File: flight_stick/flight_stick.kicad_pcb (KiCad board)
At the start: 2 copper layers, 75 x 50 mm, 61 parts, among them J1 Load Cell 1, J10 USB_C_Receptacle_USB2.0, J11 Conn_01x05_Pin, J3 Load Cell 2, J5 Load Cell 3, J7 Conn_01x04_Male, J8 Conn_01x05_Pin, J9 Conn_ST_STDC14, Q4 2N7002, Q5 2N7002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

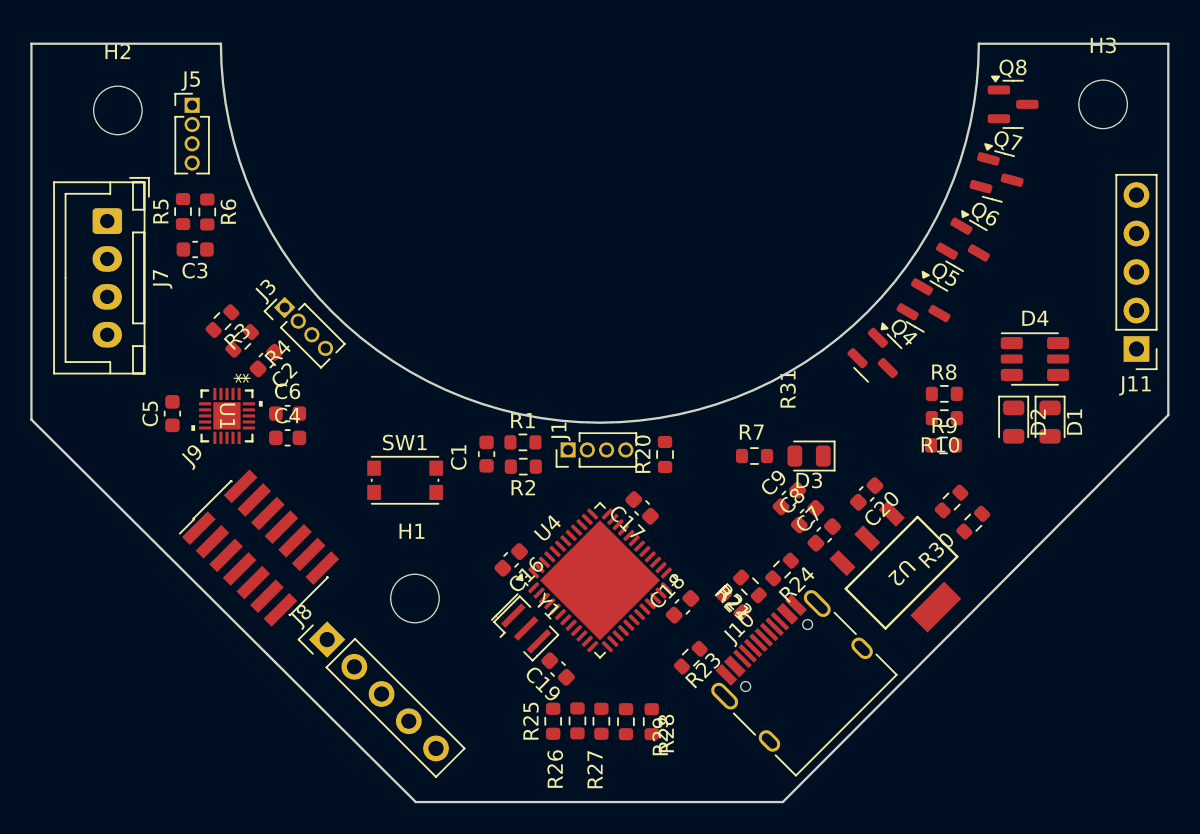
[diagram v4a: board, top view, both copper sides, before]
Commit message: Started on the Routing
layout component placement requires review, traces placed
MCU pins re-assigned
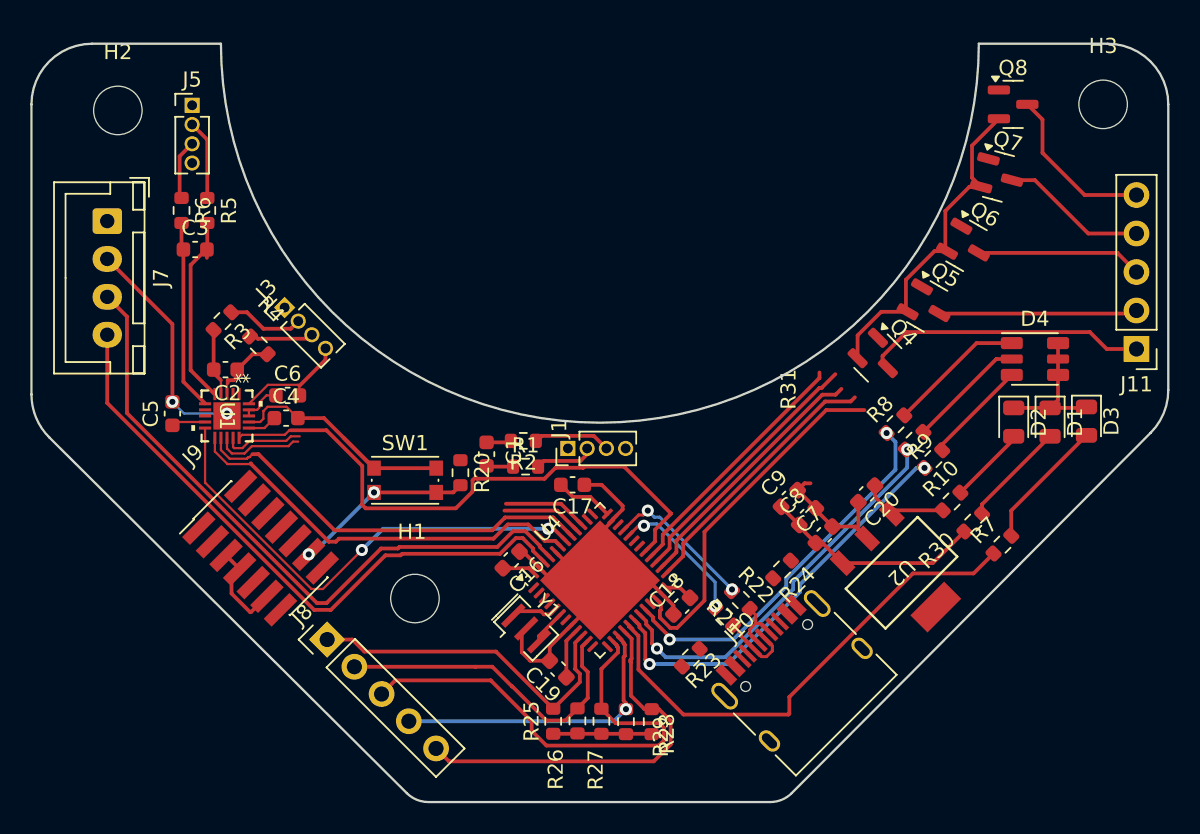
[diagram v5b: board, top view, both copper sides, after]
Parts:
- moved D3 18.4 mm to (179.6, 129.9), turned to -90 degrees
- moved R7 17.4 mm to (174.1, 138.0), turned to 45 degrees
- moved R20 13.6 mm to (138.3, 133.3), turned to -90 degrees
- moved C17 4.83 mm to (145.7, 134.1), turned to 180 degrees
- moved R8 3.79 mm to (167.0, 130.1), turned to 45 degrees
- moved C2 2.77 mm to (122.8, 126.5), turned to 180 degrees
- moved R9 2.47 mm to (168.3, 131.2), turned to 45 degrees
- moved R6 1.70 mm to (119.9, 116.0)
- moved R2 1.70 mm to (142.4, 131.2)
- moved R1 1.61 mm to (142.6, 132.9)
- moved R5 1.60 mm to (121.6, 116.0), turned to -90 degrees
- moved C4 1.30 mm to (126.8, 129.7)
- moved C6 1.20 mm to (126.9, 128.2)
- moved R4 1.14 mm to (125.0, 124.9), turned to -45 degrees
- moved R10 1.13 mm to (169.5, 132.4), turned to 45 degrees
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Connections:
- U4 pad 18: /StatusLED_{B} -> /StatusLED_{G}
- U4 pad 20: /StatusLED_{G} -> /StatusLED_{B}
- U4 pad 22: /Trans1 -> /Trans5
- U4 pad 25: /Trans2 -> /Trans4
- U4 pad 27: /Trans4 -> /Trans2
- U4 pad 28: /Trans5 -> /Trans1
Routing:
- net GND: track 0.00 -> 123.2 mm, vias 0 -> 2
- net /SCL: track 0.00 -> 44.0 mm
- net /SDA: track 0.00 -> 41.7 mm
- net /ADC_MCK: track 0.00 -> 38.5 mm
- net +3.3V: track 0.00 -> 37.3 mm
- net Net-(U4-PA7): track 0.00 -> 32.9 mm
- net /ADC_CS: track 0.00 -> 32.3 mm, vias 0 -> 2
- net /button3: track 0.00 -> 31.8 mm
- net /ADC_DRDY: track 0.00 -> 27.3 mm
- net /ADC_SDI: track 0.00 -> 27.2 mm
- net /StatusLED_{G}: track 0.00 -> 27.1 mm, vias 0 -> 2
- net /StatusLED_{R}: track 0.00 -> 26.1 mm, vias 0 -> 2
- net /button5: track 0.00 -> 25.7 mm
- net /StatusLED_{B}: track 0.00 -> 25.2 mm, vias 0 -> 2
- net /Trans5: track 0.00 -> 23.8 mm
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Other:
- outline, holes or cut-outs redrawn

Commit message: Completed First Draft
Completed Routing
Checked DRC
Fixed All DRC issues
Did not resolve ADC clearance issues
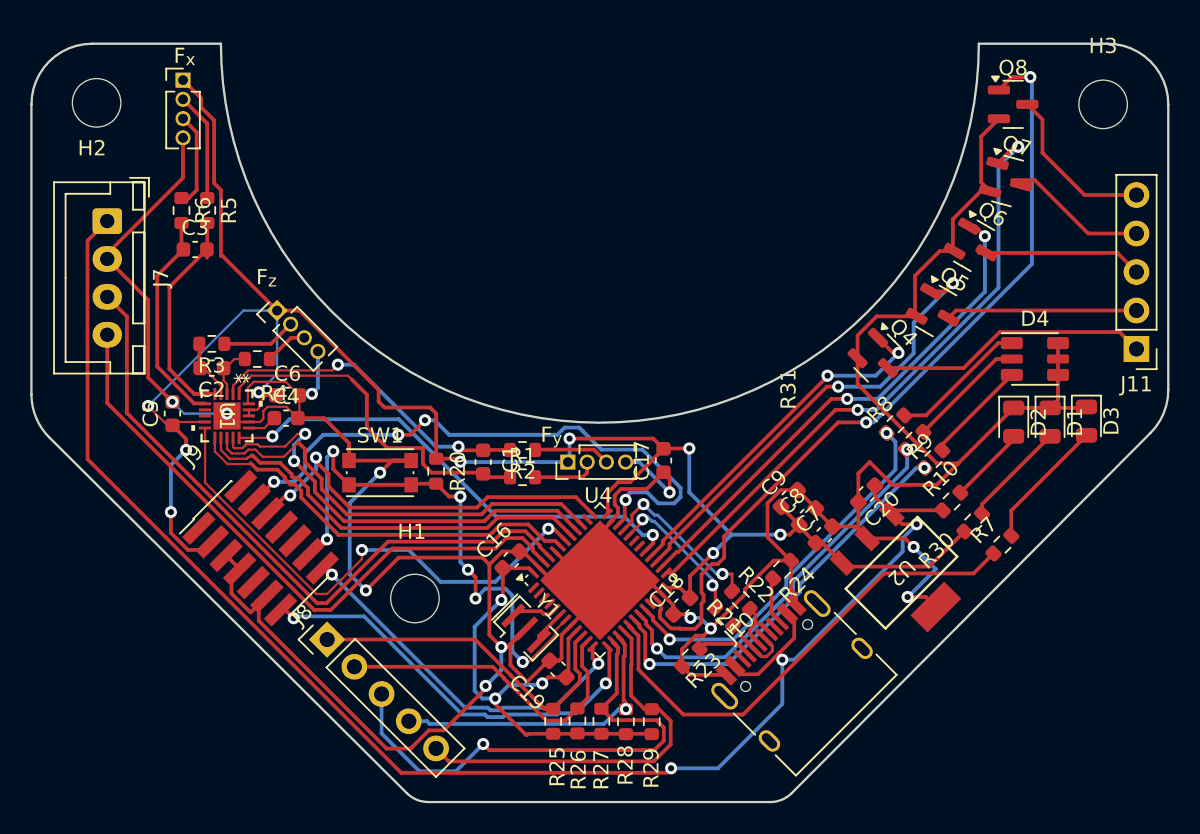
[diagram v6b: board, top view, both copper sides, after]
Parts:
- moved C17 6.21 mm to (151.7, 132.5), turned to 90 degrees
- moved F_{x} 1.77 mm to (120.0, 107.4)
- moved SW1 1.72 mm to (133.0, 133.3)
- moved R3 1.66 mm to (121.9, 124.8), turned to 180 degrees
- moved R20 1.60 mm to (136.7, 133.2)
- moved H2 1.49 mm to (114.3, 108.9)
- moved C2 0.91 mm to (121.9, 126.4)
- moved R4 0.91 mm to (124.9, 125.8), turned to 180 degrees
- moved F_{y} 0.90 mm to (145.4, 132.6)
- moved R1 0.73 mm to (142.4, 133.6)
- moved Q5 0.67 mm to (169.7, 122.6)
- moved Q7 0.67 mm to (174.4, 114.1)
- moved R2 0.60 mm to (142.4, 131.8)
- moved C1 0.57 mm to (139.8, 132.6)
- moved F_{z} 0.54 mm to (126.2, 122.6)
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- renumbered J5 to F_{x}, J1 to F_{y}, J3 to F_{z}
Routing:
- net GND: track 123.2 -> 261.4 mm, vias 2 -> 12
- net +3.3V: track 37.3 -> 162.4 mm, vias 0 -> 12
- net +5V: track 5.77 -> 103.6 mm, vias 0 -> 3
- net /codeio: track 0.00 -> 40.1 mm, vias 0 -> 4
- net /Trans5: track 23.8 -> 53.8 mm, vias 0 -> 2
- net /Programming_{RX}: track 0.00 -> 28.0 mm, vias 0 -> 2
- net /codeclk: track 0.00 -> 26.2 mm, vias 0 -> 2
- net /mcureset: track 11.9 -> 36.9 mm, vias 2 -> 6
- net /Programming_{TX}: track 0.00 -> 24.7 mm, vias 0 -> 2
- net /Trans4: track 17.7 -> 41.4 mm, vias 0 -> 2
- net Net-(U1-AIN0P): track 1.62 -> 23.3 mm
- net Net-(U1-AIN0N): track 1.57 -> 21.8 mm, vias 0 -> 2
- net /ADC_SDO: track 10.7 -> 29.7 mm, vias 0 -> 2
- net /ADC_SCK: track 11.5 -> 28.7 mm
- net /Trans3: track 17.2 -> 33.9 mm, vias 0 -> 2
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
